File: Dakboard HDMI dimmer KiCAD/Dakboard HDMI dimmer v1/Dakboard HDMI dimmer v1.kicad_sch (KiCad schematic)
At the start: 13 parts, among them J1 Conn_02x20_Odd_Even, J2 Conn_01x05, J3 Conn_01x03

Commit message: Board routing, cleanup, jlcpcb export
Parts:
- added H1, H2, H3, H4: MountingHole_Pad, MountingHole:MountingHole_2.5mm_Pad, symbol Mechanical:MountingHole_Pad
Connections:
- net GND: now also H1.1, H2.1, H3.1, H4.1
- net SCL: now also R4.2
- net SDA: now also R5.2
- net at J2.3 (Pin_3), R2.2: no longer R4.2
- net at J2.4 (Pin_4), R3.2: no longer R5.2
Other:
- note added: "40-pin"
- note added: "Connectors"
- note added: "Mounting holes"
- company: (none) -> DotaPie
- title: (none) -> Dakboard HDMI dimmer
- moved on the sheet: C2, C3, C4, C5, J1, J2, J3, R1, R2, R3, R4, R5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

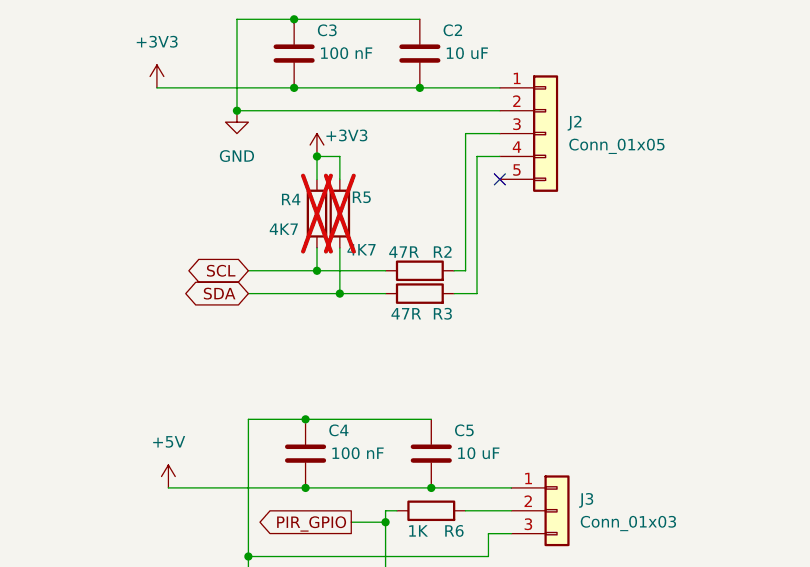
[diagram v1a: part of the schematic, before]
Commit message: Changed R I2C protective to 100R (was 47R)
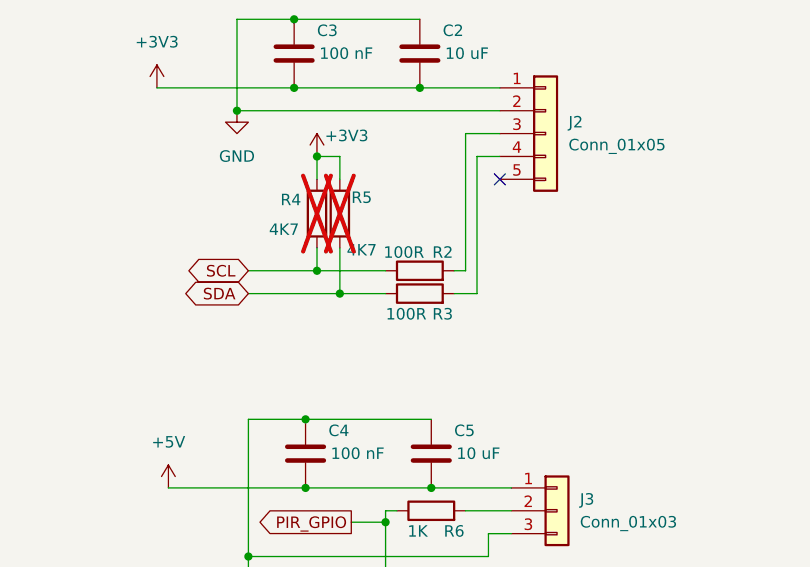
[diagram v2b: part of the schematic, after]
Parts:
- R2, R3: value 47R -> 100R
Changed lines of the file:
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@@
 			)
 		)
-		(property "Value" "47R"
+		(property "Value" "100R"
 			(at 228.346 67.056 90)
 			(show_name no)
@@
 			)
 		)
-		(property "Value" "47R"
+		(property "Value" "100R"
 			(at 228.092 60.198 90)
 			(show_name no)
